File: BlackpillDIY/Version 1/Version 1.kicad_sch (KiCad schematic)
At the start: 7 parts, among them U1 STM32F411CCUx, Y1 32.768KHz 6pF, Y2 25MHZ 9pF

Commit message: Added everything according to official schem
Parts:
- removed Y1: 32.768KHz 6pF, symbol Device:Crystal
- added C5, C6: 100n, symbol Device:C
- added C7: 2.2u, symbol Device:C
- added J1: Left Header, symbol Connector_Generic:Conn_01x10
- added J2: Right Header, symbol Connector_Generic:Conn_01x10
- added J3: Debug, symbol Connector_Generic:Conn_01x04
- added R1, R2: 10k, symbol Device:R
- added SW1: Reset Switch, Button_Switch_THT:SW_PUSH_6mm_H4.3mm, symbol Switch:SW_Push
- C1, C2: value 1.5p -> 100n
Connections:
- net GND: now also U1.23 (VSS), U1.35 (VSS), U1.47 (VSS), U1.49 (VSS), U1.8 (VSSA), C7.1, J1.4 (Pin_4), J1.8 (Pin_8), J2.4 (Pin_4), J3.4 (Pin_4), R1.1, R2.1, SW1.1; no longer C2.1
- net at C2.2: now also U1.24 (VDD), U1.36 (VDD), U1.48 (VDD), C5.2, C6.2; no longer U1.28 (PB15)
- net at C1.2: now also U1.7 (NRST), SW1.2; no longer U1.27 (PB14)
- net TIM2_CH1: now reaches U1.10 (PA0)
- net TIM2_CH1: now also J1.1 (Pin_1)
- net TIM2_CH2: now reaches U1.11 (PA1)
- net TIM2_CH2: now also J1.2 (Pin_2)
- net TIM2_CH3: now reaches U1.12 (PA2)
- net TIM2_CH3: now also U1.13 (PA3), J1.3 (Pin_3)
- net PotMeter: now reaches U1.14 (PA4)
- net PotMeter: now also J1.10 (Pin_10)
- net at U1.20 (PB2): now also R2.2
- net I2C2_SCL: now reaches U1.21 (PB10)
- net I2C2_SCL: now also J1.7 (Pin_7)
- net at U1.22 (VCAP1): now also C7.2
- net TIM1_CH1N: now reaches U1.26 (PB13)
- net TIM1_CH1N: now also J2.9 (Pin_9)
- net TIM1_CH1: now reaches U1.29 (PA8)
- net TIM1_CH1: now also J2.10 (Pin_10)
- net TIM1_CH2: now reaches U1.30 (PA9)
- net TIM1_CH2: now also J2.8 (Pin_8)
- net TIM1_CH3: now reaches U1.31 (PA10)
- net TIM1_CH3: now also J2.6 (Pin_6)
- net at U1.34 (PA13): now also J3.2 (Pin_2)
- net at U1.37 (PA14): now also J3.3 (Pin_3)
- net I2C2_SDA: now reaches U1.39 (PB3)
- net I2C2_SDA: now also J1.6 (Pin_6)
- net EXTI4: now reaches U1.40 (PB4)
- net EXTI4: now also J1.9 (Pin_9)
- net I2C1_SCL: now reaches U1.42 (PB6)
- net I2C1_SCL: now also J2.3 (Pin_3)
- net I2C1_SDA: now reaches U1.43 (PB7)
- net I2C1_SDA: now also J2.2 (Pin_2)
- net at U1.44 (BOOT0): now also R1.2
- new net +3.3V: C2.1, C5.1, C6.1, J1.5 (Pin_5), J2.1 (Pin_1), J3.1 (Pin_1)
- new net TIM1_CH2N: J2.7 (Pin_7), U1.27 (PB14)
- new net TIM1_CH3N: J2.5 (Pin_5), U1.28 (PB15)
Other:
- moved on the sheet: C3, C4, Y2

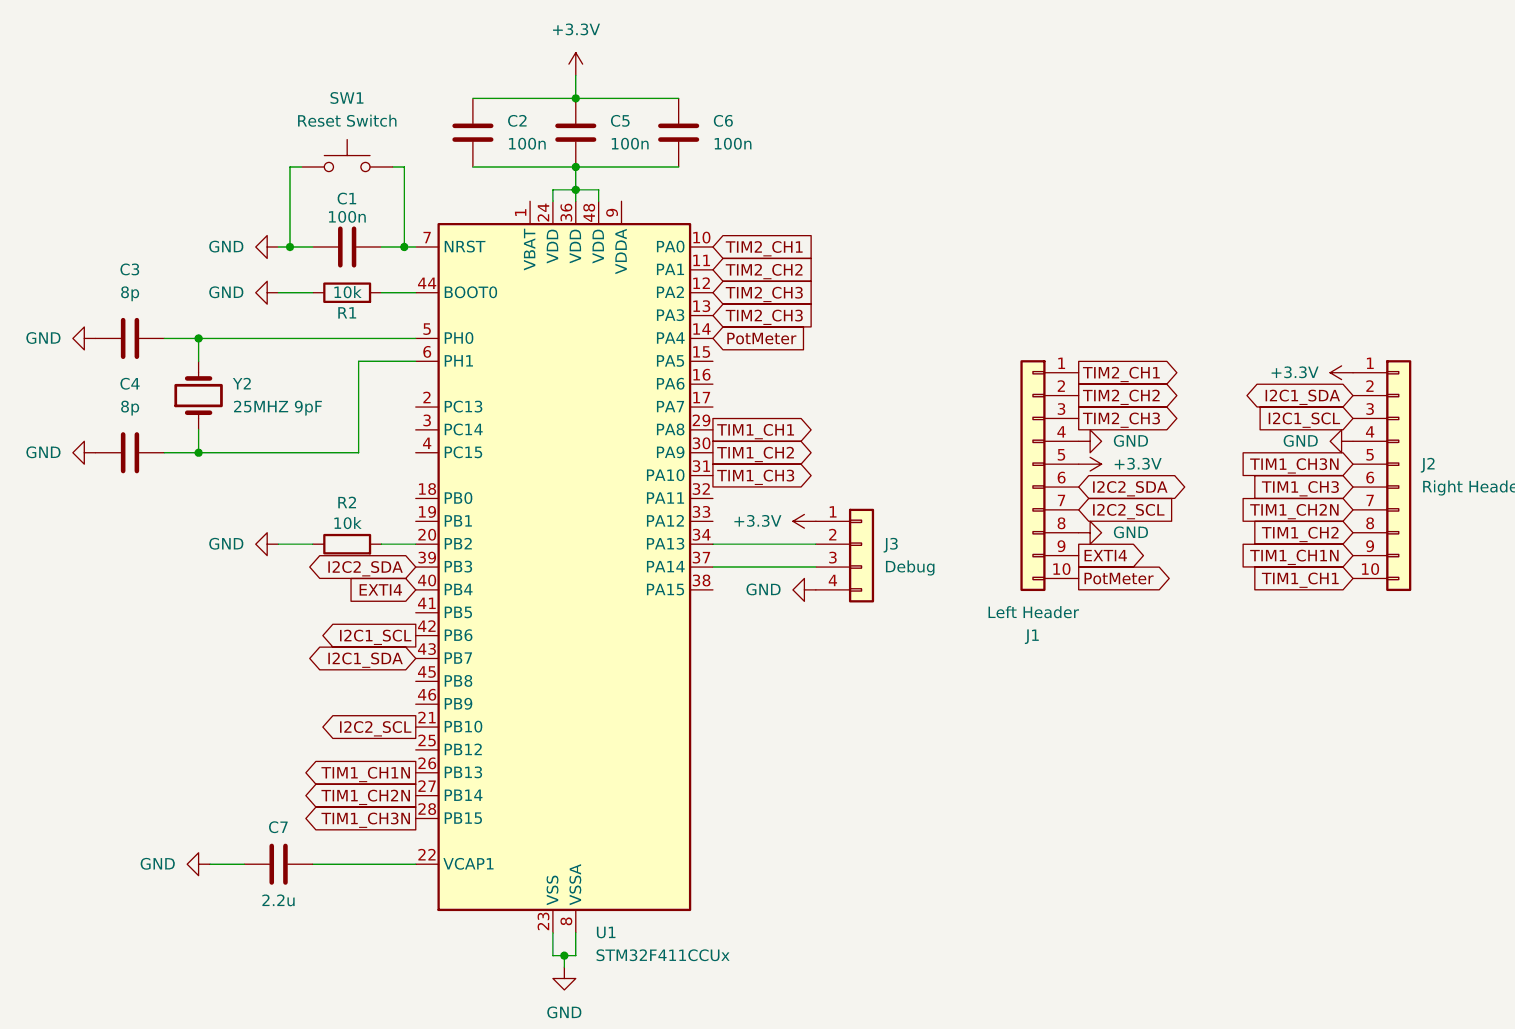
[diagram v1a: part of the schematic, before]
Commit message: Created THT PCB
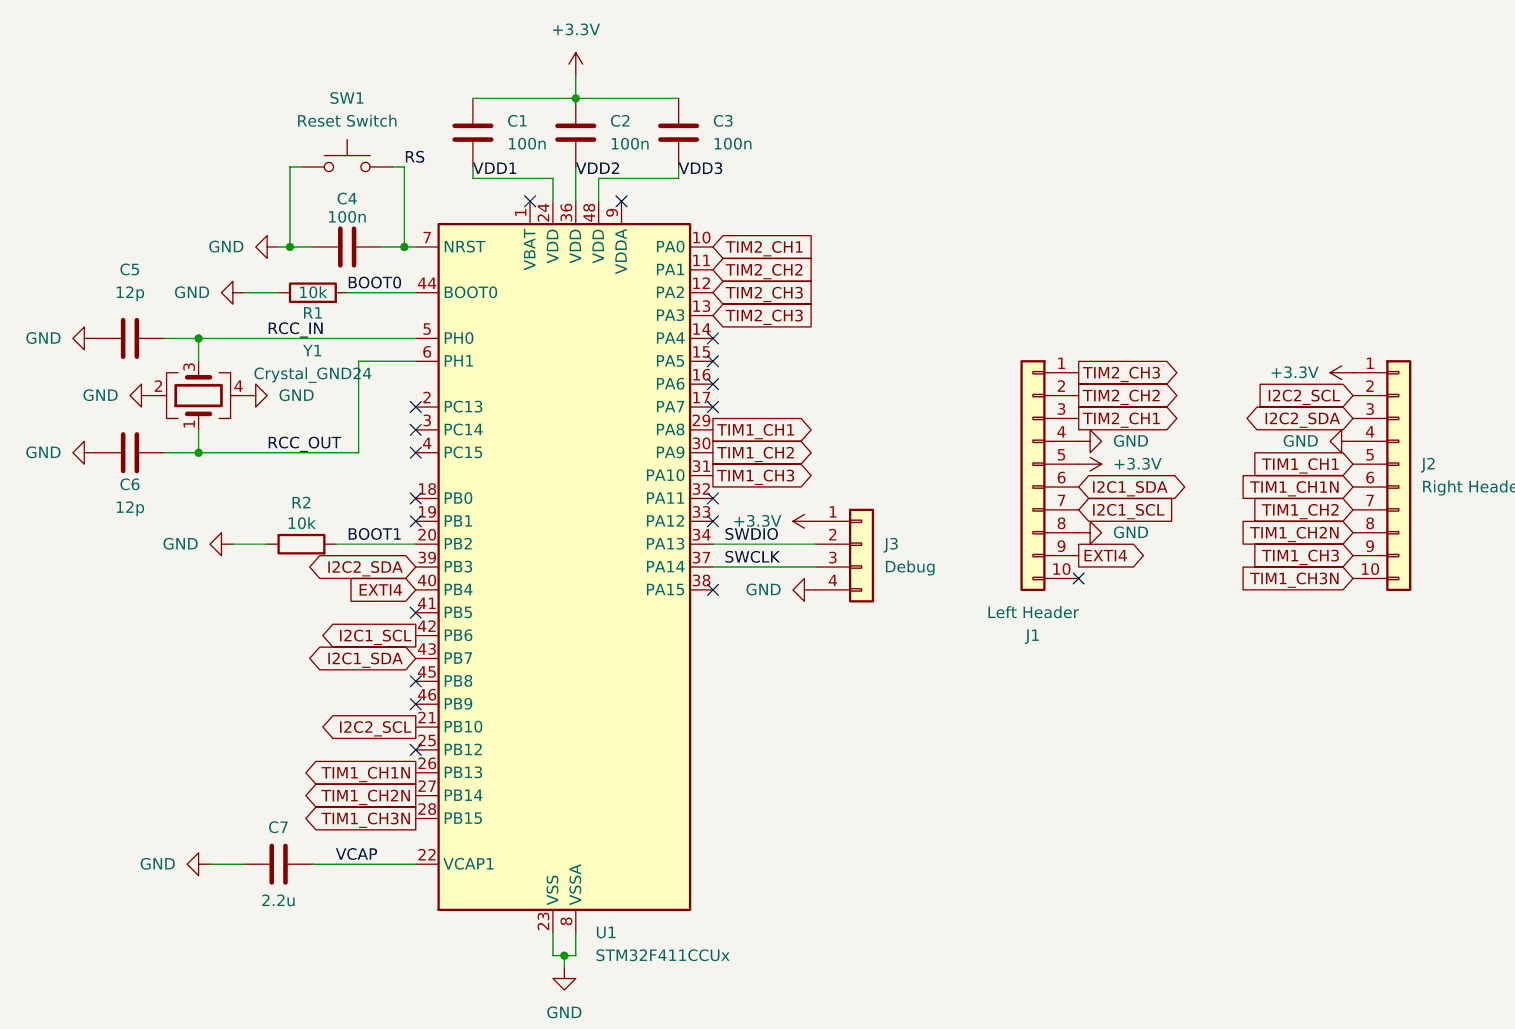
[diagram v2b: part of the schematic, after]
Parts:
- removed Y2: 25MHZ 9pF, symbol Device:Crystal
- added Y1: Crystal_GND24, Crystal:Crystal_SMD_SeikoEpson_FA128-4Pin_2.0x1.6mm, symbol Device:Crystal_GND24
- C1: renamed from C6; footprint (none) -> Capacitor_THT:C_Disc_D5.0mm_W2.5mm_P5.00mm
- C2: footprint (none) -> Capacitor_THT:C_Disc_D5.0mm_W2.5mm_P5.00mm
- C3: renamed from C5; footprint (none) -> Capacitor_THT:C_Disc_D5.0mm_W2.5mm_P5.00mm
- C4: renamed from C1; footprint (none) -> Capacitor_THT:C_Disc_D5.0mm_W2.5mm_P5.00mm
- C5: renamed from C3; value 8p -> 12p; footprint (none) -> Capacitor_SMD:C_0603_1608Metric
- C6: renamed from C4; value 8p -> 12p; footprint (none) -> Capacitor_SMD:C_0603_1608Metric
- C7: footprint (none) -> Capacitor_THT:CP_Radial_D5.0mm_P2.00mm
- J1, J2: footprint (none) -> Connector_PinHeader_2.54mm:PinHeader_1x10_P2.54mm_Vertical
- J3: footprint (none) -> Connector_PinHeader_2.54mm:PinHeader_1x04_P2.54mm_Vertical
- R1, R2: footprint (none) -> Resistor_THT:R_Axial_DIN0207_L6.3mm_D2.5mm_P10.16mm_Horizontal
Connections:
- net GND: now also Y1.2, Y1.4
- net I2C1_SCL: now also J1.7 (Pin_7); no longer J2.3 (Pin_3)
- net I2C1_SDA: now also J1.6 (Pin_6); no longer J2.2 (Pin_2)
- net I2C2_SCL: now also J2.2 (Pin_2); no longer J1.7 (Pin_7)
- net I2C2_SDA: now also J2.3 (Pin_3); no longer J1.6 (Pin_6)
- net TIM1_CH1: now also J2.5 (Pin_5); no longer J2.10 (Pin_10)
- net TIM1_CH1N: now also J2.6 (Pin_6); no longer J2.9 (Pin_9)
- net TIM1_CH2: now also J2.7 (Pin_7); no longer J2.8 (Pin_8)
- net TIM1_CH2N: now also J2.8 (Pin_8); no longer J2.7 (Pin_7)
- net TIM1_CH3: now also J2.9 (Pin_9); no longer J2.6 (Pin_6)
- net TIM1_CH3N: now also J2.10 (Pin_10); no longer J2.5 (Pin_5)
- net TIM2_CH1: now also J1.3 (Pin_3); no longer J1.1 (Pin_1)
- net TIM2_CH3: now also J1.1 (Pin_1); no longer J1.3 (Pin_3)
- net RS: now reaches C4.2, SW1.2, U1.7 (NRST)
- net BOOT0: now reaches R1.2, U1.44 (BOOT0)
- net RCC_IN: now reaches C5.2, U1.5 (PH0)
- net RCC_IN: now also Y1.3
- net RCC_OUT: now reaches C6.2, U1.6 (PH1)
- net RCC_OUT: now also Y1.1
- net SWDIO: now reaches J3.2 (Pin_2), U1.34 (PA13)
- net SWCLK: now reaches J3.3 (Pin_3), U1.37 (PA14)
- net BOOT1: now reaches R2.2, U1.20 (PB2)
- net VCAP: now reaches C7.2, U1.22 (VCAP1)
- net PotMeter: no longer names the net of U1.14 (PA4)
- net PotMeter: no longer J1.10 (Pin_10)
- new net VDD1: C1.2, U1.24 (VDD)
- new net VDD2: C2.2, U1.36 (VDD)
- new net VDD3: C3.2, U1.48 (VDD)
- no-connect marks 0 -> 19
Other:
- moved on the sheet: C1, C2, C3, R1, R2
